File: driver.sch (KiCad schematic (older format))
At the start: 54 parts, among them U10 LM5008MM, U11 SN74LVC1G66DBVR, U12 LM5107, U13 SN74LVC1G66DBVR, U14 AQY282S, U15 LM5107, U17 LMR12010YMKE_NOPB, U2 SN74LVC1G66DBVR, U3 LM5107

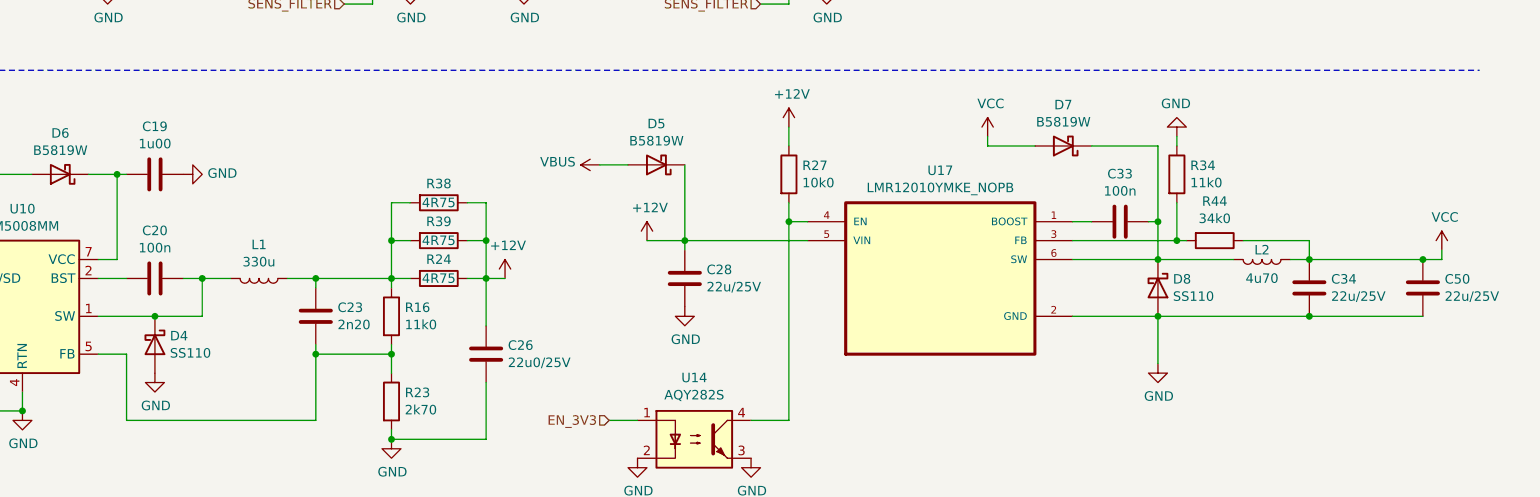
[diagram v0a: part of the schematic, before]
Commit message: - remove solder-mask from bottom layer
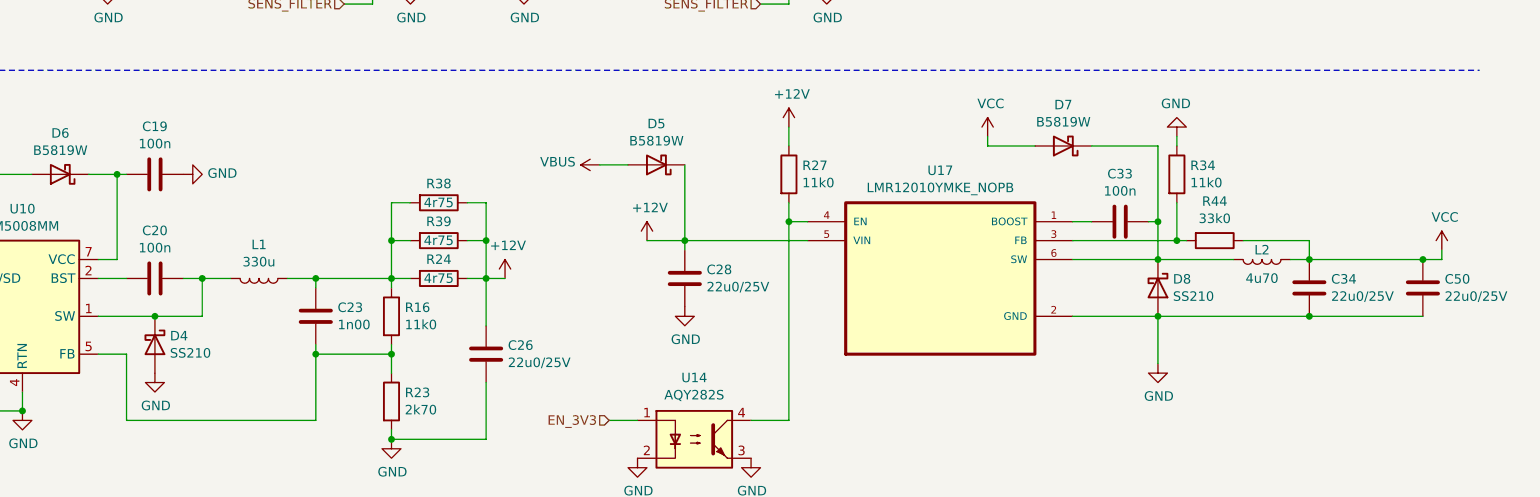
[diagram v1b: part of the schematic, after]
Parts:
- C19: value 1u00 -> 100n
- C23: value 2n20 -> 1n00
- C28, C34, C50: value 22u/25V -> 22u0/25V
- D4, D8: value SS110 -> SS210
- D5, D6, D7: LCSC (none) -> C8598
- L1: LCSC C169382 -> C169381; Partnumber SWRB1207S-471MT -> SWRB1207S-331MT
- L2: footprint Inductor_SMD:L_Wuerth_WE-PD2-Typ-L -> Inductor_SMD:L_Sunlord_MWSA0518_5.4x5.2mm; LCSC C169382 -> C408410; Partnumber SWRB1207S-471MT -> MWSA0503S-4R7MT
- R24, R38, R39: value 4R75 -> 4r75
- R27: value 10k0 -> 11k0
- R44: value 34k0 -> 33k0
- U10: LCSC (none) -> C9424
- U11, U13, U2: LCSC (none) -> C133643
- U12, U15, U3: LCSC (none) -> C132096
- U14: LCSC (none) -> C250827
- U17: LCSC (none) -> C57930
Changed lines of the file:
@@
 F 2 "Package_SO:SOIC-8_3.9x4.9mm_P1.27mm" H 2100 800 50  0001 C CIN
 F 3 "" H 2100 1300 50  0001 C CNN
+F 4 "C132096" H 2100 1300 50  0001 C CNN "LCSC"
 	1    2100 1300
 	1    0    0    -1
@@
 F 2 "Package_SO:SOIC-8_3.9x4.9mm_P1.27mm" H 4800 800 50  0001 C CIN
 F 3 "" H 4800 1300 50  0001 C CNN
+F 4 "C132096" H 4800 1300 50  0001 C CNN "LCSC"
 	1    4800 1300
 	1    0    0    -1
@@
 F 2 "Package_SO:SOIC-8_3.9x4.9mm_P1.27mm" H 7450 800 50  0001 C CIN
 F 3 "" H 7450 1300 50  0001 C CNN
+F 4 "C132096" H 7450 1300 50  0001 C CNN "LCSC"
 	1    7450 1300
 	1    0    0    -1
@@
 F 2 "gesc:M74VHC1GT66DTT1G" H 6200 3350 60  0001 C CNN
 F 3 "" H 5700 3550 60  0000 C CNN
+F 4 "C133643" H 5700 3550 50  0001 C CNN "LCSC"
 	1    5700 3550
 	1    0    0    -1
@@
 F 2 "gesc:M74VHC1GT66DTT1G" H 4000 3350 60  0001 C CNN
 F 3 "" H 3500 3550 60  0000 C CNN
+F 4 "C133643" H 3500 3550 50  0001 C CNN "LCSC"
 	1    3500 3550
 	1    0    0    -1
@@
 F 2 "gesc:M74VHC1GT66DTT1G" H 1700 3350 60  0001 C CNN
 F 3 "" H 1200 3550 60  0000 C CNN
+F 4 "C133643" H 1200 3550 50  0001 C CNN "LCSC"
 	1    1200 3550
 	1    0    0    -1
@@
 P 5150 4900
 F 0 "R38" V 5050 4900 50  0000 C CNN
-F 1 "4R75" V 5150 4900 50  0000 C CNN
+F 1 "4r75" V 5150 4900 50  0000 C CNN
 F 2 "Resistor_SMD:R_0805_2012Metric" V 5080 4900 50  0001 C CNN
 F 3 "~" H 5150 4900 50  0001 C CNN
@@
 P 5150 5100
 F 0 "R39" V 5050 5100 50  0000 C CNN
-F 1 "4R75" V 5150 5100 50  0000 C CNN
+F 1 "4r75" V 5150 5100 50  0000 C CNN
 F 2 "Resistor_SMD:R_0805_2012Metric" V 5080 5100 50  0001 C CNN
 F 3 "~" H 5150 5100 50  0001 C CNN
@@
 P 3650 5650
 F 0 "D4" V 3604 5729 50  0000 L CNN
-F 1 "SS110" V 3695 5729 50  0000 L CNN
+F 1 "SS210" V 3695 5729 50  0000 L CNN
 F 2 "Diode_SMD:D_SMA" H 3650 5475 50  0001 C CNN
 F 3 "http://www.jameco.com/Jameco/Products/ProdDS/1538777.pdf" H 3650 5650 50  0001 C CNN
@@
 P 4500 5500
 F 0 "C23" H 4615 5546 50  0000 L CNN
-F 1 "2n20" H 4615 5455 50  0000 L CNN
+F 1 "1n00" H 4615 5455 50  0000 L CNN
 F 2 "Capacitor_SMD:C_0805_2012Metric" H 4538 5350 50  0001 C CNN
 F 3 "~" H 4500 5500 50  0001 C CNN
@@
 P 5150 5300
 F 0 "R24" V 5050 5300 50  0000 C CNN
-F 1 "4R75" V 5150 5300 50  0000 C CNN
+F 1 "4r75" V 5150 5300 50  0000 C CNN
 F 2 "Resistor_SMD:R_0805_2012Metric" V 5080 5300 50  0001 C CNN
 F 3 "~" H 5150 5300 50  0001 C CNN
@@
 F 2 "Inductor_SMD:L_12x12mm_H4.5mm" H 4200 5300 50  0001 C CNN
 F 3 "~" H 4200 5300 50  0001 C CNN
-F 4 "SWRB1207S-471MT" V 4200 5300 50  0001 C CNN "Partnumber"
-F 5 "C169382" V 4200 5300 50  0001 C CNN "LCSC"
+F 4 "SWRB1207S-331MT" V 4200 5300 50  0001 C CNN "Partnumber"
+F 5 " C169381" V 4200 5300 50  0001 C CNN "LCSC"
 	1    4200 5300
 	0    1    1    0
@@
 P 3650 4750
 F 0 "C19" V 3902 4750 50  0000 C CNN
-F 1 "1u00" V 3811 4750 50  0000 C CNN
+F 1 "100n" V 3811 4750 50  0000 C CNN
 F 2 "Capacitor_SMD:C_0805_2012Metric" H 3688 4600 50  0001 C CNN
 F 3 "~" H 3650 4750 50  0001 C CNN
@@
 F 2 "Package_SO:MSOP-8_3x3mm_P0.65mm" H 3000 4950 50  0001 L CIN
 F 3 "http://www.ti.com/lit/ds/symlink/lm5008.pdf" H 2950 5400 50  0001 C CNN
+F 4 " C9424" H 2950 5400 50  0001 C CNN "LCSC"
 	1    2950 5400
 	1    0    0    -1
@@
 F 2 "gesc:SOT95P280X110-6N" H 7800 5300 50  0001 L BNN
 F 3 "" H 7800 5300 50  0001 L BNN
+F 4 " C57930" H 7800 5300 50  0001 C CNN "LCSC"
 	1    7800 5300
 	1    0    0    -1
@@
 P 6450 5300
 F 0 "C28" H 6565 5346 50  0000 L CNN
-F 1 "22u/25V" H 6565 5255 50  0000 L CNN
+F 1 "22u0/25V" H 6565 5255 50  0000 L CNN
 F 2 "Capacitor_SMD:C_0805_2012Metric" H 6488 5150 50  0001 C CNN
 F 3 "~" H 6450 5300 50  0001 C CNN
@@
 P 8950 5350
 F 0 "D8" V 8904 5429 50  0000 L CNN
-F 1 "SS110" V 8995 5429 50  0000 L CNN
+F 1 "SS210" V 8995 5429 50  0000 L CNN
 F 2 "Diode_SMD:D_SMA" H 8950 5175 50  0001 C CNN
 F 3 "http://www.jameco.com/Jameco/Products/ProdDS/1538777.pdf" H 8950 5350 50  0001 C CNN
@@
 F 0 "L2" V 9450 5200 50  0000 C CNN
 F 1 "4u70" V 9600 5200 50  0000 C CNN
-F 2 "Inductor_SMD:L_Wuerth_WE-PD2-Typ-L" H 9500 5200 50  0001 C CNN
+F 2 "Inductor_SMD:L_Sunlord_MWSA0518_5.4x5.2mm" H 9500 5200 50  0001 C CNN
 F 3 "~" H 9500 5200 50  0001 C CNN
-F 4 "SWRB1207S-471MT" V 9500 5200 50  0001 C CNN "Partnumber"
-F 5 "C169382" V 9500 5200 50  0001 C CNN "LCSC"
+F 4 "MWSA0503S-4R7MT" V 9500 5200 50  0001 C CNN "Partnumber"
+F 5 " C408410" V 9500 5200 50  0001 C CNN "LCSC"
 	1    9500 5200
 	0    1    1    0
@@
 P 9750 5350
 F 0 "C34" H 9865 5396 50  0000 L CNN
-F 1 "22u/25V" H 9865 5305 50  0000 L CNN
+F 1 "22u0/25V" H 9865 5305 50  0000 L CNN
 F 2 "Capacitor_SMD:C_0805_2012Metric" H 9788 5200 50  0001 C CNN
 F 3 "~" H 9750 5350 50  0001 C CNN
@@
 P 10350 5350
 F 0 "C50" H 10465 5396 50  0000 L CNN
-F 1 "22u/25V" H 10465 5305 50  0000 L CNN
+F 1 "22u0/25V" H 10465 5305 50  0000 L CNN
 F 2 "Capacitor_SMD:C_0805_2012Metric" H 10388 5200 50  0001 C CNN
 F 3 "~" H 10350 5350 50  0001 C CNN
@@
 P 9250 5100
 F 0 "R44" V 9043 5100 50  0000 C CNN
-F 1 "34k0" V 9134 5100 50  0000 C CNN
+F 1 "33k0" V 9134 5100 50  0000 C CNN
 F 2 "Resistor_SMD:R_0805_2012Metric" V 9180 5100 50  0001 C CNN
 F 3 "~" H 9250 5100 50  0001 C CNN
@@
 F 2 "Package_SO:SO-4_4.4x4.3mm_P2.54mm" H 6300 5950 50  0001 L CIN
 F 3 "http://www.vishay.com/docs/83740/sfh617a.pdf" H 6500 6150 50  0001 L CNN
+F 4 "C250827" H 6500 6150 50  0001 C CNN "LCSC"
 	1    6500 6150
 	1    0    0    -1
@@
 P 7000 4750
 F 0 "R27" H 7070 4796 50  0000 L CNN
-F 1 "10k0" H 7070 4705 50  0000 L CNN
+F 1 "11k0" H 7070 4705 50  0000 L CNN
 F 2 "Resistor_SMD:R_0805_2012Metric" V 6930 4750 50  0001 C CNN
 F 3 "~" H 7000 4750 50  0001 C CNN
@@
 F 2 "Diode_SMD:D_SOD-123" H 6300 4700 50  0001 C CNN
 F 3 "~" H 6300 4700 50  0001 C CNN
+F 4 "C8598" H 6300 4700 50  0001 C CNN "LCSC"
 	1    6300 4700
 	-1   0    0    1
@@
 F 2 "Diode_SMD:D_SOD-123" H 8450 4600 50  0001 C CNN
 F 3 "~" H 8450 4600 50  0001 C CNN
+F 4 "C8598" H 8450 4600 50  0001 C CNN "LCSC"
 	1    8450 4600
 	-1   0    0    1
@@
 F 2 "Diode_SMD:D_SOD-123" H 3150 4750 50  0001 C CNN
 F 3 "~" H 3150 4750 50  0001 C CNN
+F 4 "C8598" H 3150 4750 50  0001 C CNN "LCSC"
 	1    3150 4750
 	-1   0    0    1

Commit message: BUGS ergänzt
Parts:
- added D? (x6): TVS, symbol Diode:B360
- added D? (x3): SS210, Diode_SMD:D_SMA, symbol Diode:B360
- added R? (x3): 5r60, symbol Device:R
- C21, C27, C32: value 100n -> 10u0/25V
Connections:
- wire segments 206 -> 240
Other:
- moved on the sheet: C15, C21, C22, C27, C29, C32

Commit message: |--- Add Schottky between phase and gnd at HS pin of LM5107 |--- Add 5R6 in phase line to HS pin of LM5107 |--- Change high side bypass cap to 10u/25V |--- Add 14V TVS diode parallel to high side bypass cap |--- Add one 12V TVS diode to 12V near driver |--- move gate tracks and back from side by side to on top of each other
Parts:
- removed D? (x6): TVS, symbol Diode:B360
- added D13, D14, D15: SMF14A, Diode_SMD:D_SOD-123F, symbol Diode:1.5KExxA
- added D16: SMF12A, Diode_SMD:D_SOD-123F, symbol Diode:1.5KExxA
- D10, D12, D9: renamed from D?; value SS210 -> MBR2H100SFTN; footprint Diode_SMD:D_SMA -> Diode_SMD:D_SOD-123
- R47, R48, R49: renamed from R?; footprint (none) -> Resistor_SMD:R_0805_2012Metric
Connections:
- net labels added: SH_A_R, SH_B_R, SH_C_R
- wire segments 240 -> 231

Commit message: Version mit UCC27211
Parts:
- removed U12, U15, U3: LM5107, Package_SO:SOIC-8_3.9x4.9mm_P1.27mm, symbol gesc:LM5107
- added D17, D18, D19, D20, D21: SMF14A, Diode_SMD:D_SOD-123F, symbol Diode:1.5KExxA
- added D22, D23, D24: SMF58A, Diode_SMD:D_SOD-123F, symbol Diode:1.5KExxA
- added U12, U15, U3: UCC27211, Package_SO:SOIC-8_3.9x4.9mm_P1.27mm, symbol gesc:UCC27211
- D16: value SMF12A -> SMF14A; LCSC C178259 -> C523839
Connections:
- wire segments 231 -> 250
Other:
- moved on the sheet: C15, C21, C22, C27, C29, C32, D10, D12, D9, R21, R22, R47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

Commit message: save
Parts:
- removed D10, D12, D9: MBR2H100SFTN, Diode_SMD:D_SOD-123, symbol Diode:B360
- removed D13, D14, D15, D16, D17, D18, D19, D20, D21: SMF14A, Diode_SMD:D_SOD-123F, symbol Diode:1.5KExxA
- removed D22, D23, D24: SMF58A, Diode_SMD:D_SOD-123F, symbol Diode:1.5KExxA
- removed R47, R48, R49: 5r60, Resistor_SMD:R_0805_2012Metric, symbol Device:R
- removed U12, U15, U3: UCC27211, Package_SO:SOIC-8_3.9x4.9mm_P1.27mm, symbol gesc:UCC27211
- added U12, U15, U3: 2ED2304S06F, Package_SO:SOIC-8_3.9x4.9mm_P1.27mm, symbol gesc:2ED2304S06F
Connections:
- net labels removed: SH_A_R, SH_B_R, SH_C_R
- wire segments 250 -> 206

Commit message: - new driver 2ED2304S06F - separat Elkos for each phase - new FET placement
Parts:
- added C55, C57, C58: 100n, Capacitor_SMD:C_0805_2012Metric, symbol Device:C
- L1: footprint Inductor_SMD:L_12x12mm_H4.5mm -> Inductor_SMD:L_6.3x6.3_H3; LCSC C169381 -> C83453; Partnumber SWRB1207S-331MT -> SWPA6045S331MT
- L2: value 4u70 -> 15u0; footprint Inductor_SMD:L_Sunlord_MWSA0518_5.4x5.2mm -> Inductor_SMD:L_6.3x6.3_H3; LCSC C408410 -> C83374; Partnumber MWSA0503S-4R7MT -> SWPA6045S150MT
- U17: value LMR12010YMKE_NOPB -> LMR12010YMKE
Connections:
- net +12V: now also C55.1, C57.1, C58.1
- net GND: now also C55.2, C57.2, C58.2
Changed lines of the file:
@@
 F 0 "L1" V 4022 5300 50  0000 C CNN
 F 1 "330u" V 4113 5300 50  0000 C CNN
-F 2 "Inductor_SMD:L_12x12mm_H4.5mm" H 4200 5300 50  0001 C CNN
+F 2 "Inductor_SMD:L_6.3x6.3_H3" H 4200 5300 50  0001 C CNN
 F 3 "~" H 4200 5300 50  0001 C CNN
-F 4 "SWRB1207S-331MT" V 4200 5300 50  0001 C CNN "Partnumber"
-F 5 " C169381" V 4200 5300 50  0001 C CNN "LCSC"
+F 4 "SWPA6045S331MT" V 4200 5300 50  0001 C CNN "Partnumber"
+F 5 " C83453" V 4200 5300 50  0001 C CNN "LCSC"
 	1    4200 5300
 	0    1    1    0
@@
 P 7800 5300
 F 0 "U17" H 7800 5870 50  0000 C CNN
-F 1 "LMR12010YMKE_NOPB" H 7800 5779 50  0000 C CNN
+F 1 "LMR12010YMKE" H 7800 5779 50  0000 C CNN
 F 2 "gesc:SOT95P280X110-6N" H 7800 5300 50  0001 L BNN
 F 3 "" H 7800 5300 50  0001 L BNN
@@
 P 9500 5200
 F 0 "L2" V 9450 5200 50  0000 C CNN
-F 1 "4u70" V 9600 5200 50  0000 C CNN
-F 2 "Inductor_SMD:L_Sunlord_MWSA0518_5.4x5.2mm" H 9500 5200 50  0001 C CNN
+F 1 "15u0" V 9600 5200 50  0000 C CNN
+F 2 "Inductor_SMD:L_6.3x6.3_H3" H 9500 5200 50  0001 C CNN
 F 3 "~" H 9500 5200 50  0001 C CNN
-F 4 "MWSA0503S-4R7MT" V 9500 5200 50  0001 C CNN "Partnumber"
-F 5 " C408410" V 9500 5200 50  0001 C CNN "LCSC"
+F 4 "SWPA6045S150MT" V 9500 5200 50  0001 C CNN "Partnumber"
+F 5 "C83374" V 9500 5200 50  0001 C CNN "LCSC"
 	1    9500 5200
 	0    1    1    0
@@
 Wire Wire Line
 	2700 1450 3050 1450
+$Comp
+L Device:C C55
+U 1 1 604AE3ED
+P 650 1150
+F 0 "C55" H 765 1196 50  0000 L CNN
+F 1 "100n" H 765 1105 50  0000 L CNN
+F 2 "Capacitor_SMD:C_0805_2012Metric" H 688 1000 50  0001 C CNN
+F 3 "~" H 650 1150 50  0001 C CNN
+	1    650  1150
+	1    0    0    -1
+$EndComp
+Wire Wire Line
+	650  1000 650  950
+Wire Wire Line
+	650  950  850  950
+Wire Wire Line
+	650  1300 650  1550
+Wire Wire Line
+	650  1550 850  1550
+$Comp
+L Device:C C57
+U 1 1 604C80EB
+P 3850 1150
+F 0 "C57" H 3965 1196 50  0000 L CNN
+F 1 "100n" H 3965 1105 50  0000 L CNN
+F 2 "Capacitor_SMD:C_0805_2012Metric" H 3888 1000 50  0001 C CNN
+F 3 "~" H 3850 1150 50  0001 C CNN
+	1    3850 1150
+	1    0    0    -1
+$EndComp
+Wire Wire Line
+	3850 1000 3850 950
+Wire Wire Line
+	3850 950  4250 950
+Wire Wire Line
+	3850 1300 3850 1550
+Wire Wire Line
+	3850 1550 4250 1550
+$Comp
+L Device:C C58
+U 1 1 604E5F6C
+P 7450 1150
+F 0 "C58" H 7565 1196 50  0000 L CNN
+F 1 "100n" H 7565 1105 50  0000 L CNN
+F 2 "Capacitor_SMD:C_0805_2012Metric" H 7488 1000 50  0001 C CNN
+F 3 "~" H 7450 1150 50  0001 C CNN
+	1    7450 1150
+	1    0    0    -1
+$EndComp
+Wire Wire Line
+	7450 1000 7450 950
+Wire Wire Line
+	7450 950  7850 950
+Wire Wire Line
+	7450 1300 7450 1550
+Wire Wire Line
+	7450 1550 7850 1550
 $EndSCHEMATC

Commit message: save
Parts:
- removed C50: 22u0/25V, Capacitor_SMD:C_0805_2012Metric, symbol Device:C
- removed D7: B5819W, Diode_SMD:D_SOD-123, symbol Device:D_Schottky
- removed D8: SS210, Diode_SMD:D_SMA, symbol Diode:B360
- removed L2: 15u0, Inductor_SMD:L_6.3x6.3_H3, symbol Device:L
- removed U17: LMR12010YMKE, gesc:SOT95P280X110-6N, symbol gesc:LMR12010YMKE_NOPB
- added D7: ZPD12, Diode_SMD:D_MiniMELF, symbol Diode:ZPDxx
- added R48: 110k, Resistor_SMD:R_0805_2012Metric, symbol Device:R
- added U17: TPS82140, Package_LGA:Texas_SIL0008D_MicroSiP-8-1EP_2.8x3mm_P0.65mm_EP1.1x1.9mm, symbol Regulator_Switching:TPS82140
- C33: value 100n -> 3n30
- R15: value 100k -> 110k
- R27: value 11k0 -> 3k30
- R34: value 11k0 -> 330k
- R44: value 33k0 -> 2k10
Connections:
- net EN_3V3 is gone; now on net EN_12V: U14.1
- net +12V: now also U17.2 (VIN); no longer R27.1
- net EN_12V: now also R44.2; no longer R12.1, U10.6 (RON/SD)
- net GND: now also C33.2, D7.2 (A), R48.2, U17.3 (GND), U17.9 (GND); no longer R34.1
- net VBAT: now also R27.2
- net VCC: now also R34.1, U17.4 (VOUT), U17.5 (VOUT); no longer R44.1
- net at U14.4: now also R12.1, U10.6 (RON/SD); no longer R27.2
- net at C33.1: now also U17.8 (SS/TR)
- net at R34.2: now also R48.1, U17.6 (FB); no longer R44.2
- new net V_AUX: D7.1 (K), R27.1, R44.1
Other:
- moved on the sheet: C28, C34, D5, R34, U14
